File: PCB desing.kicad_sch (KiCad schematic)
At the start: 39 parts, among them J1 Conn_01x02_Socket, J2 Conn_01x02_Pin, J3 Conn_01x02_Pin, J4 Conn_01x02_Socket, U1 LM2735X, U1 STM32L476RGTx, U1 TPS63001DRC, U2 FGPMMOPA6H, U8 LM386

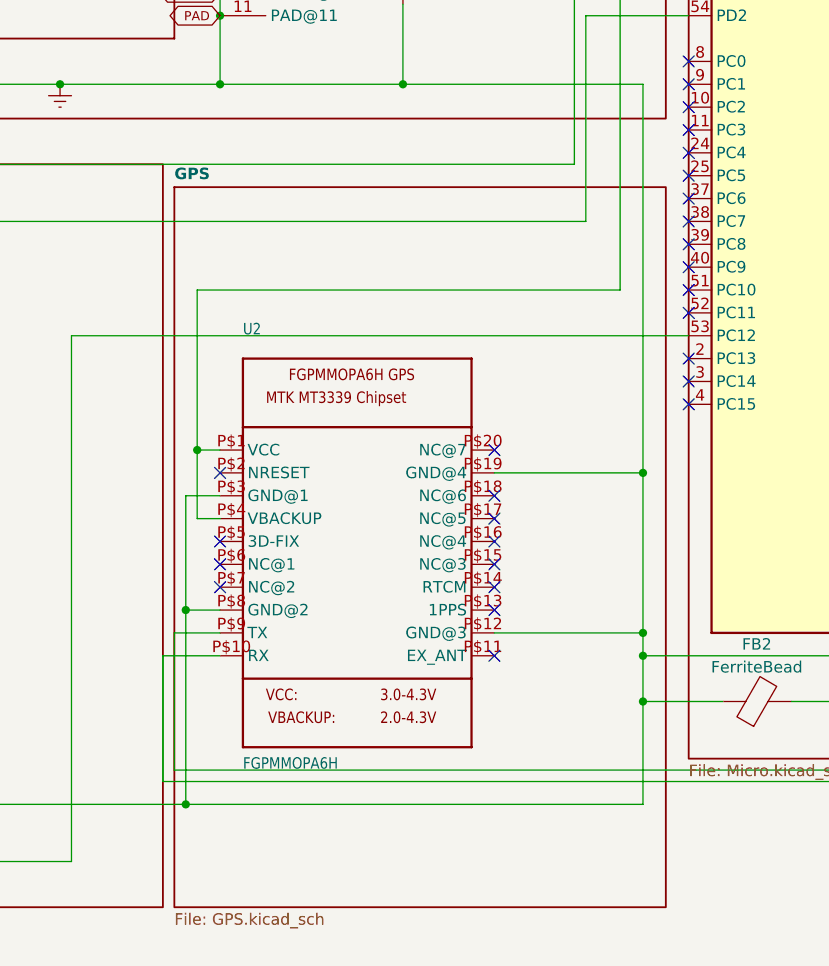
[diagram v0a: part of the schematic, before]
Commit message: Updated the indivdual components.
Some of the individual components still need to be updated and completed. With the battery box, include the diode. The full schematic is not the update one as Andrew has the updated one with the correct flyback diode placement.
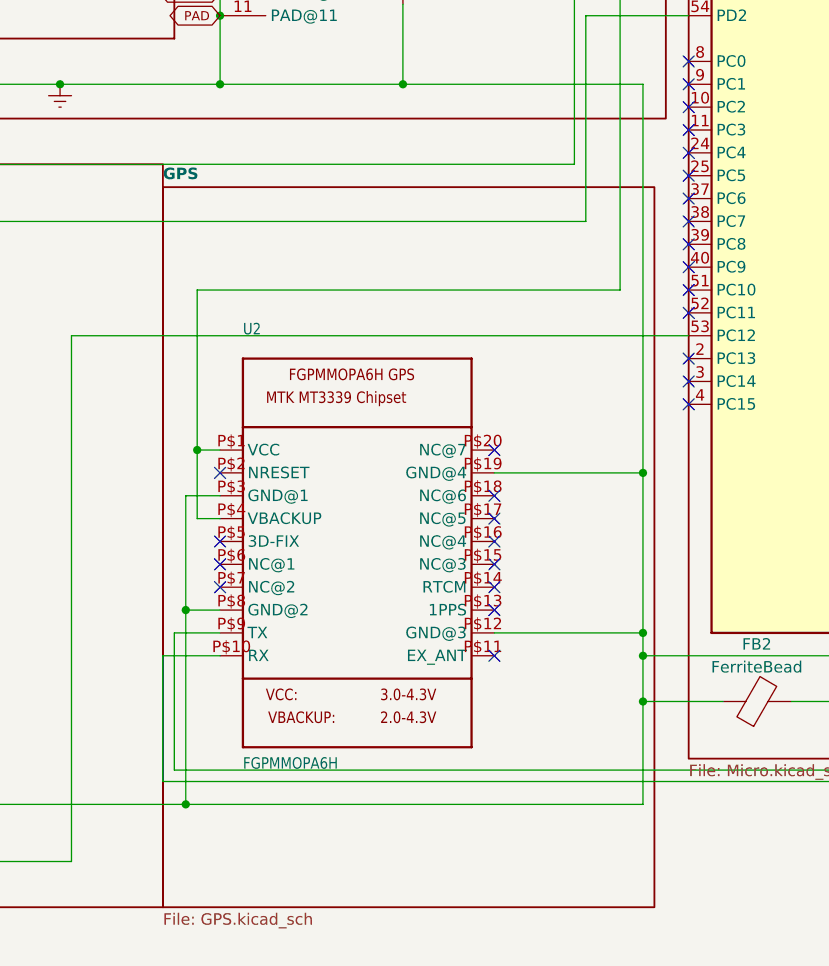
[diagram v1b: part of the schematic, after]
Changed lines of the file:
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@@
 		)
 		(instances
-			(project "PCB"
+			(project "PCB desing"
 				(path "/eb9a8801-b205-4599-90e8-b0089b4de1f9"
 					(page "6")
@@
 		)
 		(instances
-			(project "PCB"
+			(project "PCB desing"
 				(path "/eb9a8801-b205-4599-90e8-b0089b4de1f9"
 					(page "7")
@@
 		)
 		(instances
-			(project "PCB"
+			(project "PCB desing"
 				(path "/eb9a8801-b205-4599-90e8-b0089b4de1f9"
 					(page "5")
@@
 		)
 		(instances
-			(project "PCB"
+			(project "PCB desing"
 				(path "/eb9a8801-b205-4599-90e8-b0089b4de1f9"
 					(page "8")
@@
 	)
 	(sheet
-		(at 93.98 114.3)
+		(at 92.71 114.3)
 		(size 54.61 80.01)
 		(fields_autoplaced yes)
@@
 		)
 		(property "Sheetname" "GPS"
-			(at 93.98 113.563 0)
+			(at 92.71 113.563 0)
 			(effects
 				(font
@@
 		)
 		(property "Sheetfile" "GPS.kicad_sch"
-			(at 93.98 194.92 0)
-			(effects
-				(font
-					(size 1.27 1.27)
-				)
-				(justify left top)
-			)
-		)
-		(instances
-			(project "PCB"
+			(at 92.71 194.92 0)
+			(effects
+				(font
+					(size 1.27 1.27)
+				)
+				(justify left top)
+			)
+		)
+		(instances
+			(project "PCB desing"
 				(path "/eb9a8801-b205-4599-90e8-b0089b4de1f9"
 					(page "4")
@@
 		)
 		(instances
-			(project "PCB"
+			(project "PCB desing"
 				(path "/eb9a8801-b205-4599-90e8-b0089b4de1f9"
 					(page "3")
@@
 		)
 		(instances
-			(project "PCB"
+			(project "PCB desing"
 				(path "/eb9a8801-b205-4599-90e8-b0089b4de1f9"
 					(page "2")

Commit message: Add files via upload
Finished everything except for the micro schematic
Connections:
- net at C1.1, C3.1, L2.1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: now also D1.1 (K); no longer J2.2 (Pin_2)
- net at BT1.1 (+): now also J1.2 (Pin_2); no longer D1.2 (A)
- new net: D1.2 (A), J2.2 (Pin_2)
- no-connect marks 62 -> 60
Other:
- sheet Baterry Box renamed Battery Box
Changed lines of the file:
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@@
 	)
 	(junction
-		(at 19.05 27.94)
-		(diameter 0)
-		(color 0 0 0 0)
-	)
-	(junction
 		(at 243.84 39.37)
 		(diameter 0)
@@
 	)
 	(junction
+		(at 19.05 35.56)
+		(diameter 0)
+		(color 0 0 0 0)
+	)
+	(junction
 		(at 204.47 67.31)
 		(diameter 0)
@@
 	)
 	(no_connect
-		(at 151.13 90.17)
-	)
-	(no_connect
 		(at 186.69 143.51)
 	)
@@
 	)
 	(no_connect
-		(at 151.13 87.63)
-	)
-	(no_connect
 		(at 151.13 118.11)
 	)
@@
 	(wire
 		(pts
-			(xy -27.94 -6.35) (xy -27.94 15.24)
+			(xy -27.94 -24.13) (xy -27.94 15.24)
 		)
 		(stroke
@@
 	(wire
 		(pts
-			(xy 160.02 27.94) (xy 160.02 17.78)
+			(xy 160.02 35.56) (xy 160.02 17.78)
 		)
 		(stroke
@@
 	(wire
 		(pts
+			(xy 15.24 35.56) (xy 19.05 35.56)
+		)
+		(stroke
+			(width 0)
+			(type default)
+		)
+	)
+	(wire
+		(pts
 			(xy 99.06 62.23) (xy 104.14 62.23)
 		)
@@
 	(wire
 		(pts
-			(xy -27.94 -24.13) (xy -27.94 -13.97)
-		)
-		(stroke
-			(width 0)
-			(type default)
-		)
-	)
-	(wire
-		(pts
 			(xy 168.91 72.39) (xy 171.45 72.39)
 		)
@@
 	(wire
 		(pts
-			(xy 19.05 27.94) (xy 160.02 27.94)
+			(xy 19.05 35.56) (xy 160.02 35.56)
 		)
 		(stroke
@@
 	(wire
 		(pts
-			(xy 15.24 27.94) (xy 15.24 67.31)
-		)
-		(stroke
-			(width 0)
-			(type default)
-		)
-	)
-	(wire
-		(pts
 			(xy 160.02 67.31) (xy 157.48 67.31)
 		)
@@
 	(wire
 		(pts
+			(xy 15.24 35.56) (xy 15.24 67.31)
+		)
+		(stroke
+			(width 0)
+			(type default)
+		)
+	)
+	(wire
+		(pts
 			(xy 195.58 17.78) (xy 209.55 17.78)
 		)
@@
 	(wire
 		(pts
-			(xy -15.24 -24.13) (xy -27.94 -24.13)
+			(xy -27.94 -24.13) (xy -15.24 -24.13)
 		)
 		(stroke
@@
 	(wire
 		(pts
-			(xy 15.24 27.94) (xy 19.05 27.94)
-		)
-		(stroke
-			(width 0)
-			(type default)
-		)
-	)
-	(wire
-		(pts
 			(xy 15.24 67.31) (xy 43.18 67.31)
 		)
@@
 	)
 	(symbol
-		(lib_id "Device:D")
-		(at -27.94 -10.16 90)
-		(unit 1)
-		(exclude_from_sim no)
-		(in_bom yes)
-		(on_board yes)
-		(dnp no)
-		(fields_autoplaced yes)
-		(property "Reference" "D1"
-			(at -24.13 -10.795 90)
-			(effects
-				(font
-					(size 1.27 1.27)
-				)
-				(justify right)
-			)
-		)
-		(property "Value" "D"
-			(at -24.13 -8.255 90)
-			(effects
-				(font
-					(size 1.27 1.27)
-				)
-				(justify right)
-			)
-		)
-		(property "Footprint" ""
-			(at -27.94 -10.16 0)
-			(effects
-				(font
-					(size 1.27 1.27)
-				)
-				(hide yes)
-			)
-		)
-		(property "Datasheet" "~"
-			(at -27.94 -10.16 0)
-			(effects
-				(font
-					(size 1.27 1.27)
-				)
-				(hide yes)
-			)
-		)
-		(property "Description" ""
-			(at -27.94 -10.16 0)
-			(effects
-				(font
-					(size 1.27 1.27)
-				)
-				(hide yes)
-			)
-		)
-		(property "Sim.Device" "D"
-			(at -27.94 -10.16 0)
-			(effects
-				(font
-					(size 1.27 1.27)
-				)
-				(hide yes)
-			)
-		)
-		(property "Sim.Pins" "1=K 2=A"
-			(at -27.94 -10.16 0)
-			(effects
-				(font
-					(size 1.27 1.27)
-				)
-				(hide yes)
-			)
-		)
-		(pin "1"
-		)
-		(pin "2"
-		)
-		(instances
-			(project "PCB"
-				(path "/eb9a8801-b205-4599-90e8-b0089b4de1f9"
-					(reference "D1")
-					(unit 1)
-				)
-			)
-		)
-	)
-	(symbol
 		(lib_id "Device:R_US")
 		(at 243.84 57.15 0)
@@
 	)
 	(symbol
+		(lib_id "Device:D")
+		(at 19.05 31.75 90)
+		(unit 1)
+		(exclude_from_sim no)
+		(in_bom yes)
+		(on_board yes)
+		(dnp no)
+		(fields_autoplaced yes)
+		(property "Reference" "D1"
+			(at 22.86 31.115 90)
+			(effects
+				(font
+					(size 1.27 1.27)
+				)
+				(justify right)
+			)
+		)
+		(property "Value" "D"
+			(at 22.86 33.655 90)
+			(effects
+				(font
+					(size 1.27 1.27)
+				)
+				(justify right)
+			)
+		)
+		(property "Footprint" ""
+			(at 19.05 31.75 0)
+			(effects
+				(font
+					(size 1.27 1.27)
+				)
+				(hide yes)
+			)
+		)
+		(property "Datasheet" "~"
+			(at 19.05 31.75 0)
+			(effects
+				(font
+					(size 1.27 1.27)
+				)
+				(hide yes)
+			)
+		)
+		(property "Description" ""
+			(at 19.05 31.75 0)
+			(effects
+				(font
+					(size 1.27 1.27)
+				)
+				(hide yes)
+			)
+		)
+		(property "Sim.Device" "D"
+			(at 19.05 31.75 0)
+			(effects
+				(font
+					(size 1.27 1.27)
+				)
+				(hide yes)
+			)
+		)
+		(property "Sim.Pins" "1=K 2=A"
+			(at 19.05 31.75 0)
+			(effects
+				(font
+					(size 1.27 1.27)
+				)
+				(hide yes)
+			)
+		)
+		(pin "1"
+		)
+		(pin "2"
+		)
+		(instances
+			(project "PCB desing"
+				(path "/eb9a8801-b205-4599-90e8-b0089b4de1f9"
+					(reference "D1")
+					(unit 1)
+				)
+			)
+		)
+	)
+	(symbol
 		(lib_id "power:VCC")
 		(at 201.93 80.01 0)
@@
 	)
 	(sheet
-		(at 195.58 73.66)
-		(size 130.81 78.74)
+		(at 198.12 73.66)
+		(size 83.82 78.74)
 		(fields_autoplaced yes)
 		(stroke
@@
 		)
 		(property "Sheetname" "Power AMP"
-			(at 195.58 72.923 0)
+			(at 198.12 72.923 0)
 			(effects
 				(font
@@
 		)
 		(property "Sheetfile" "Power_amp.kicad_sch"
-			(at 195.58 153.01 0)
+			(at 198.12 153.01 0)
 			(effects
 				(font
@@
 	(sheet
 		(at -36.83 -40.64)
-		(size 83.82 72.39)
+		(size 96.52 81.28)
 		(fields_autoplaced yes)
 		(stroke
@@
 			(color 0 0 0 0.0000)
 		)
-		(property "Sheetname" "Baterry Box"
+		(property "Sheetname" "Battery Box"
 			(at -36.83 -41.377 0)
 			(effects
@@
 		)
 		(property "Sheetfile" "BatteryBox.kicad_sch"
-			(at -36.83 32.36 0)
+			(at -36.83 41.25 0)
 			(effects
 				(font
@@
 	)
 	(sheet
-		(at 13.97 19.05)
-		(size 134.62 87.63)
+		(at 13.97 45.72)
+		(size 134.62 60.96)
 		(fields_autoplaced yes)
 		(stroke
@@
 		)
 		(property "Sheetname" "Buck-Boost"
-			(at 13.97 18.313 0)
+			(at 13.97 44.983 0)
 			(effects
 				(font

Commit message: Add files via upload
Finished the main schematic as well as the sub schematics
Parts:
- removed C10: 5V, symbol Device:C_Polarized_Small_US
- removed U1: TPS63001DRC, Buck-Boost Converter Chip:DRC0010J, symbol 2024-09-27_13-12-33-eagle-import:TPS63001DRCRTPS63001DRCR
- removed U1: LM2735X, Boost Converter Chip:MF05A, symbol 2024-09-27_13-12-28-eagle-import:LM2735XMF/NOPBLM2735XMF/NOPB
- added C21, C22, C23, C27: .1 uF, symbol Device:C
- added C24: 4.7 uF, symbol Device:C
- added C25: .01 uF, symbol Device:C
- added C26: 1 uF, symbol Device:C
- added FB4, FB5: FerriteBead, symbol Device:FerriteBead
- added J10, J11, J12, J9: Programming Pin, symbol Connector_Generic_MountingPin:Conn_01x01_MountingPin
- added U12: MAX7375AXR805, Package_TO_SOT_SMD:SOT-323_SC-70, symbol Oscillator:MAX7375AXR805
- added U13: LM2735XMF/NOPB, Boost:MF05A, symbol Boost Chip:LM2735XMF_NOPB
- added U4: TPS63001DRCR, Buck-Boost:DRC0010J, symbol Buck-Boost Chip:TPS63001DRCR
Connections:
- net Earth is gone; now on net +3.3 VD: C1.2, C12.1, C2.2, C3.2, C5.2, C6.2, C7.2, C8.2, FB2.1, J2.1 (Pin_1), J3.1 (Pin_1), R2.2, U1.18 (VSS), U1.31 (VSS), U1.47 (VSS), U1.63 (VSS), U2.P$12 (GND@3), U2.P$19 (GND@4), U2.P$3 (GND@1), U2.P$8 (GND@2), U3.6 (GND), U8.4 (GND)
- net VCC is gone; now on an unnamed net: C12.2
- net at C1.1, C3.1, D1.1 (K)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: now also U13.5 (VIN), U4.5 (VIN), U4.6 (EN), U4.7 (PS_SYNC), U4.8 (VINA)
- net +3.3 VD: now reaches D3.2 (A), L2.2
- net +3.3 VD: now also C21.1, C21.2, C22.1, C22.2, C23.1, C23.2, C24.1, C24.2, C27.2, FB4.1, FB5.1, U12.3 (GND), U13.1 (SW), U13.2 (GND), U4.11 (PAD), U4.3 (PGND), U4.9 (GND)
- net at C2.1, FB3.1, U1.1 (VBAT)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: now also C27.1, U12.1 (V+), U4.1 (VOUT), U4.10 (FB)
- net at L1.2: now also U4.2 (L2)
- net at L1.1: now also U4.4 (L1)
- net at U1.46 (PA13): now also J9.1 (Pin_1)
- net at U1.49 (PA14): now also J10.1 (Pin_1)
- net at U1.5 (PH0): now also U12.2 (CLOCK)
- net at U1.60 (BOOT0): now also J11.1 (Pin_1)
- net at U1.7 (NRST): now also J12.1 (Pin_1)
- net at C4.1, R2.1, R3.1: now also U13.3 (FB)
- net at R1.2: now also U13.4 (EN)
- new net: C25.1, C26.1, FB4.2
- new net: C25.2, C26.2, FB5.2
- no-connect marks 60 -> 61
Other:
- note added: "Coupling Capacitors for Microcontroller"
- moved on the sheet: C1, C11, C12, C2, C3, C5, C6, C7, C8, C9, D1, FB2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
